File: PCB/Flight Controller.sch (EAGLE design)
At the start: 6 parts, among them J1 ZX62-AB-5PA(31), J2 M50-3600542R, U1 BMP390L, U2 NINA-B306, U3 LMS8117ADT-3.3, U4 BNO055

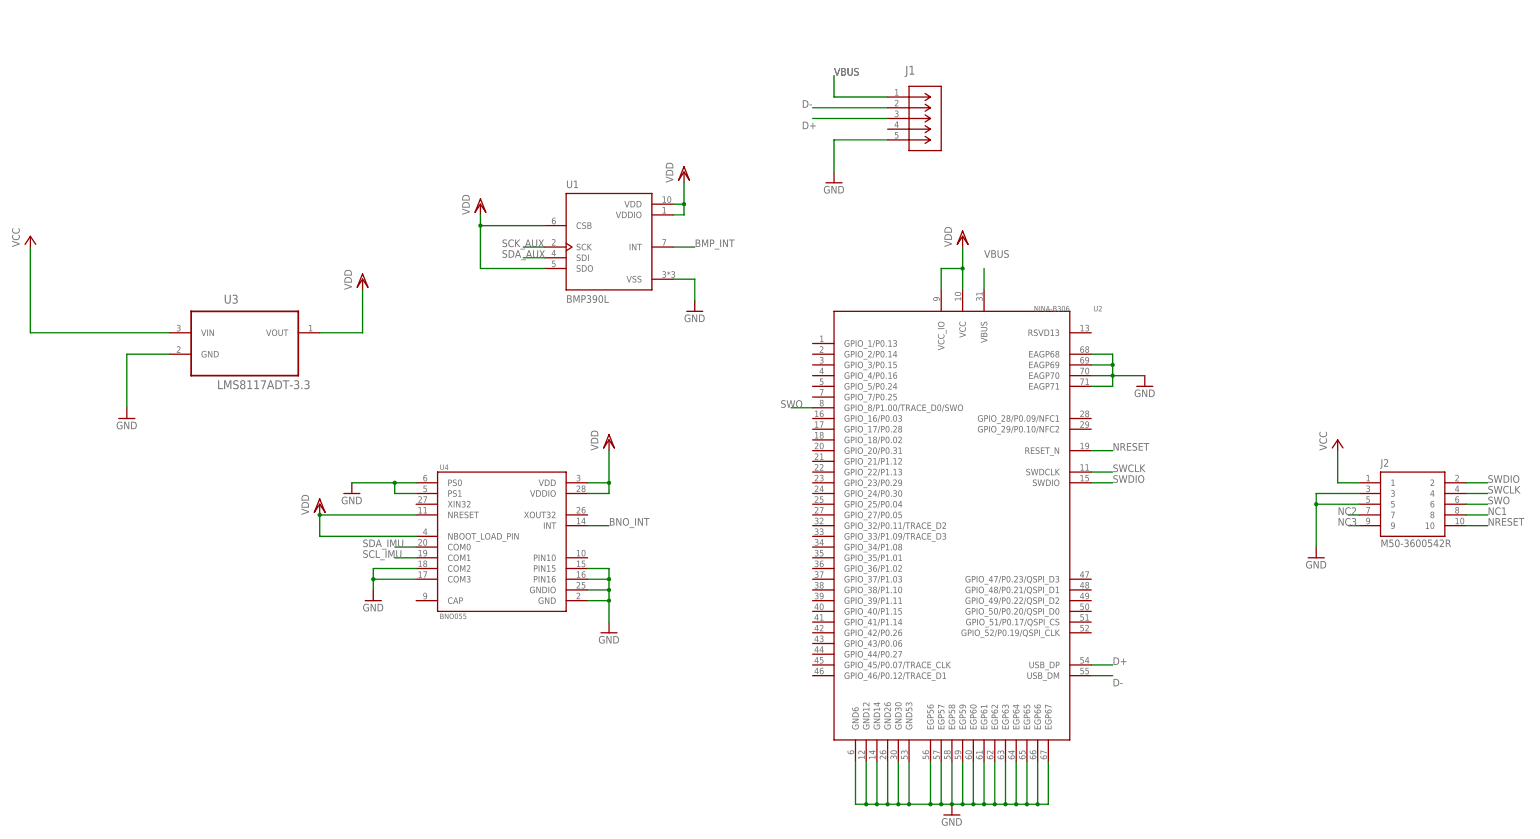
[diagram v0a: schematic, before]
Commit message: Made I2C connections on PCB
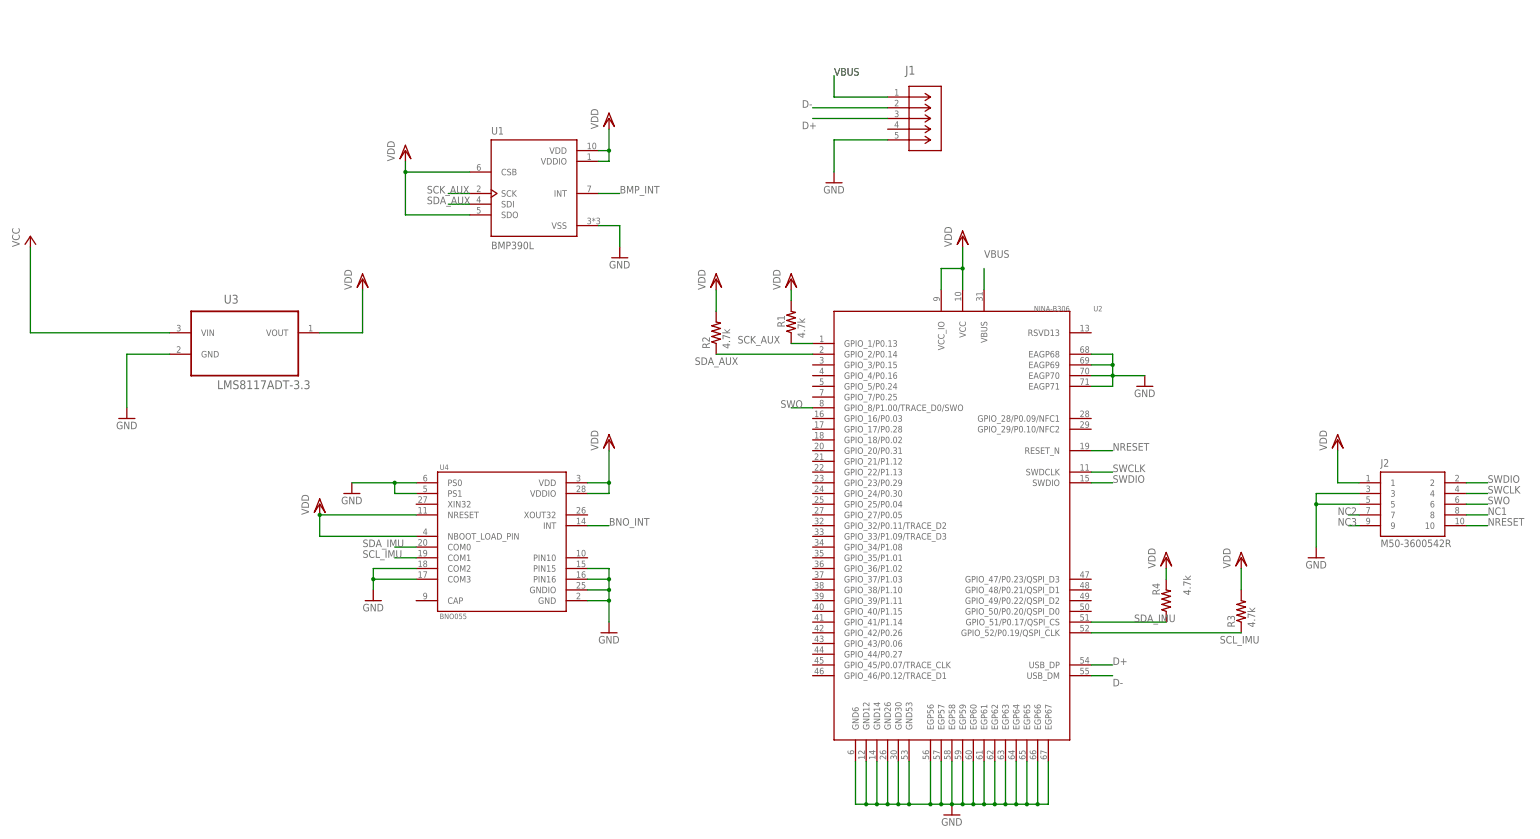
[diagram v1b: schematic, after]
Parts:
- added R1, R2, R3, R4: 4.7k, rcl:R-US_R1206
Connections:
- net SCK_AUX: now also R1.1, U2.GPIO_1/P0.13
- net SCL_IMU: now also R3.1, U2.GPIO_52/P0.19/QSPI_CLK
- net SDA_AUX: now also R2.1, U2.GPIO_2/P0.14
- net SDA_IMU: now also R4.1, U2.GPIO_51/P0.17/QSPI_CS
- net VCC: no longer J2.1
- net VDD: now also J2.1, R1.2, R2.2, R3.2, R4.2
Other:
- moved on the sheet: U1

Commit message: added UART and PWMs to NINA on schematic
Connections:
- new net PWM0: U2.GPIO_47/P0.23/QSPI_D3
- new net PWM1: U2.GPIO_48/P0.21/QSPI_D1
- new net PWM2: U2.GPIO_49/P0.22/QSPI_D2
- new net PWM3: U2.GPIO_50/P0.20/QSPI_D0
- new net UART1_RX: U2.GPIO_4/P0.16
- new net UART1_TX: U2.GPIO_3/P0.15
- new net UART2_RX: U2.GPIO_44/P0.27
- new net UART2_TX: U2.GPIO_43/P0.06
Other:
- moved on the sheet: R3, R4
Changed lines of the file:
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@@
 <attribute name="VALUE" x="297.18" y="86.36" size="1.778" layer="96" rot="R90"/>
 </instance>
-<instance part="R3" gate="G$1" x="276.86" y="48.26" smashed="yes" rot="R90">
-<attribute name="NAME" x="275.3614" y="44.45" size="1.778" layer="95" rot="R90"/>
-<attribute name="VALUE" x="280.162" y="44.45" size="1.778" layer="96" rot="R90"/>
+<instance part="R3" gate="G$1" x="287.02" y="48.26" smashed="yes" rot="R90">
+<attribute name="NAME" x="285.5214" y="44.45" size="1.778" layer="95" rot="R90"/>
+<attribute name="VALUE" x="290.322" y="44.45" size="1.778" layer="96" rot="R90"/>
 </instance>
-<instance part="R4" gate="G$1" x="259.08" y="50.8" smashed="yes" rot="R90">
-<attribute name="NAME" x="257.5814" y="52.07" size="1.778" layer="95" rot="R90"/>
-<attribute name="VALUE" x="264.922" y="52.07" size="1.778" layer="96" rot="R90"/>
+<instance part="R4" gate="G$1" x="269.24" y="50.8" smashed="yes" rot="R90">
+<attribute name="NAME" x="267.7414" y="52.07" size="1.778" layer="95" rot="R90"/>
+<attribute name="VALUE" x="275.082" y="52.07" size="1.778" layer="96" rot="R90"/>
 </instance>
-<instance part="VDD10" gate="G$1" x="259.08" y="60.96" smashed="yes">
-<attribute name="VALUE" x="256.54" y="58.42" size="1.778" layer="96" rot="R90"/>
+<instance part="VDD10" gate="G$1" x="269.24" y="60.96" smashed="yes">
+<attribute name="VALUE" x="266.7" y="58.42" size="1.778" layer="96" rot="R90"/>
 </instance>
-<instance part="VDD11" gate="G$1" x="276.86" y="60.96" smashed="yes">
-<attribute name="VALUE" x="274.32" y="58.42" size="1.778" layer="96" rot="R90"/>
+<instance part="VDD11" gate="G$1" x="287.02" y="60.96" smashed="yes">
+<attribute name="VALUE" x="284.48" y="58.42" size="1.778" layer="96" rot="R90"/>
 </instance>
 </instances>
@@
 <segment>
 <pinref part="R4" gate="G$1" pin="2"/>
-<wire x1="259.08" y1="55.88" x2="259.08" y2="58.42" width="0.1524" layer="91"/>
+<wire x1="269.24" y1="55.88" x2="269.24" y2="58.42" width="0.1524" layer="91"/>
 <pinref part="VDD10" gate="G$1" pin="VDD"/>
 </segment>
 <segment>
 <pinref part="R3" gate="G$1" pin="2"/>
-<wire x1="276.86" y1="53.34" x2="276.86" y2="58.42" width="0.1524" layer="91"/>
+<wire x1="287.02" y1="53.34" x2="287.02" y2="58.42" width="0.1524" layer="91"/>
 <pinref part="VDD11" gate="G$1" pin="VDD"/>
 </segment>
@@
 <segment>
 <pinref part="U2" gate="A" pin="GPIO_52/P0.19/QSPI_CLK"/>
-<wire x1="241.3" y1="43.18" x2="276.86" y2="43.18" width="0.1524" layer="91"/>
+<wire x1="241.3" y1="43.18" x2="287.02" y2="43.18" width="0.1524" layer="91"/>
 <pinref part="R3" gate="G$1" pin="1"/>
-<label x="271.78" y="40.64" size="1.778" layer="95"/>
+<label x="281.94" y="40.64" size="1.778" layer="95"/>
 </segment>
 </net>
@@
 <segment>
 <pinref part="U2" gate="A" pin="GPIO_51/P0.17/QSPI_CS"/>
-<wire x1="241.3" y1="45.72" x2="259.08" y2="45.72" width="0.1524" layer="91"/>
+<wire x1="241.3" y1="45.72" x2="269.24" y2="45.72" width="0.1524" layer="91"/>
 <pinref part="R4" gate="G$1" pin="1"/>
-<label x="251.46" y="45.72" size="1.778" layer="95"/>
+<label x="261.62" y="45.72" size="1.778" layer="95"/>
 </segment>
 </net>
@@
 </segment>
 </net>
+<net name="UART1_TX" class="0">
+<segment>
+<pinref part="U2" gate="A" pin="GPIO_3/P0.15"/>
+<wire x1="175.26" y1="106.68" x2="170.18" y2="106.68" width="0.1524" layer="91"/>
+<label x="162.56" y="106.68" size="1.778" layer="95"/>
+</segment>
+</net>
+<net name="UART1_RX" class="0">
+<segment>
+<pinref part="U2" gate="A" pin="GPIO_4/P0.16"/>
+<wire x1="175.26" y1="104.14" x2="170.18" y2="104.14" width="0.1524" layer="91"/>
+<label x="162.56" y="104.14" size="1.778" layer="95"/>
+</segment>
+</net>
+<net name="UART2_TX" class="0">
+<segment>
+<pinref part="U2" gate="A" pin="GPIO_43/P0.06"/>
+<wire x1="175.26" y1="40.64" x2="170.18" y2="40.64" width="0.1524" layer="91"/>
+<label x="162.56" y="40.64" size="1.778" layer="95"/>
+</segment>
+</net>
+<net name="UART2_RX" class="0">
+<segment>
+<pinref part="U2" gate="A" pin="GPIO_44/P0.27"/>
+<wire x1="175.26" y1="38.1" x2="170.18" y2="38.1" width="0.1524" layer="91"/>
+<label x="162.56" y="38.1" size="1.778" layer="95"/>
+</segment>
+</net>
+<net name="PWM0" class="0">
+<segment>
+<pinref part="U2" gate="A" pin="GPIO_47/P0.23/QSPI_D3"/>
+<wire x1="241.3" y1="55.88" x2="246.38" y2="55.88" width="0.1524" layer="91"/>
+<label x="246.38" y="55.88" size="1.778" layer="95"/>
+</segment>
+</net>
+<net name="PWM1" class="0">
+<segment>
+<pinref part="U2" gate="A" pin="GPIO_48/P0.21/QSPI_D1"/>
+<wire x1="241.3" y1="53.34" x2="246.38" y2="53.34" width="0.1524" layer="91"/>
+<label x="246.38" y="53.34" size="1.778" layer="95"/>
+</segment>
+</net>
+<net name="PWM2" class="0">
+<segment>
+<pinref part="U2" gate="A" pin="GPIO_49/P0.22/QSPI_D2"/>
+<wire x1="241.3" y1="50.8" x2="246.38" y2="50.8" width="0.1524" layer="91"/>
+<label x="246.38" y="50.8" size="1.778" layer="95"/>
+</segment>
+</net>
+<net name="PWM3" class="0">
+<segment>
+<pinref part="U2" gate="A" pin="GPIO_50/P0.20/QSPI_D0"/>
+<wire x1="241.3" y1="48.26" x2="246.38" y2="48.26" width="0.1524" layer="91"/>
+<label x="246.38" y="48.26" size="1.778" layer="95"/>
+</segment>
+</net>
